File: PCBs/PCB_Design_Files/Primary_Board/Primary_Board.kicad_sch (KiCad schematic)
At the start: 0 parts

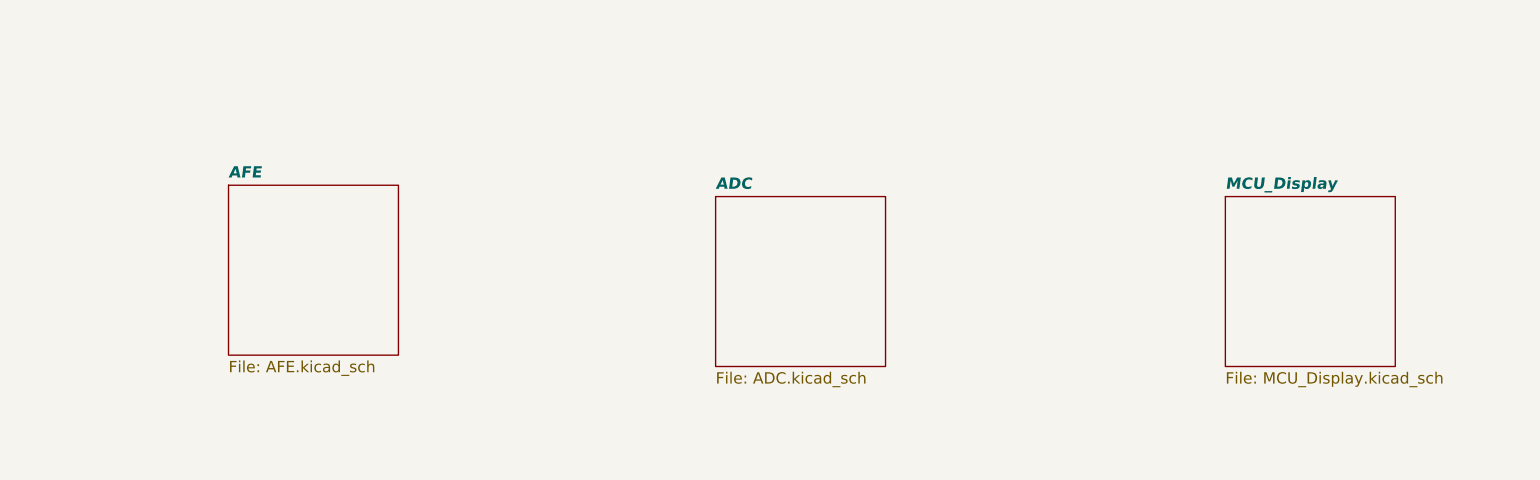
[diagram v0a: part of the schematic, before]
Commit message: AFE schematic, added 0603 component libraries
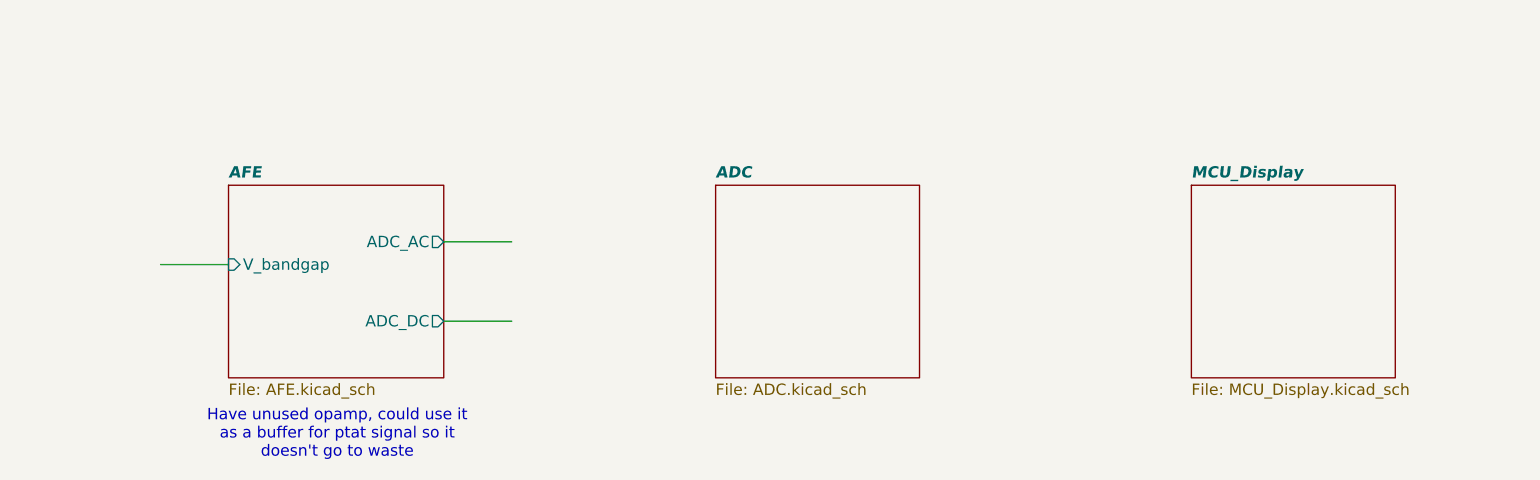
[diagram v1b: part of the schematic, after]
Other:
- sheet AFE ports: added ADC_AC, ADC_DC, V_bandgap; removed none
- note added: "Have unused opamp, could use it as a buffer for ptat signal so it doesn't go to waste"
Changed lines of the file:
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@@
 		(company "ECE115DA/DW Capstone")
+	)
+	(text "Have unused opamp, could use it\nas a buffer for ptat signal so it\ndoesn't go to waste"
+		(exclude_from_sim no)
+		(at 94.742 107.95 0)
+		(effects
+			(font
+				(size 1.27 1.27)
+			)
+		)
 	)
 	(text "Pulse Oximeter Primary Board"
@@
 		)
 	)
+	(wire
+		(pts
+			(xy 106.68 95.25) (xy 114.3 95.25)
+		)
+		(stroke
+			(width 0)
+			(type default)
+		)
+	)
+	(wire
+		(pts
+			(xy 74.93 88.9) (xy 82.55 88.9)
+		)
+		(stroke
+			(width 0)
+			(type default)
+		)
+	)
+	(wire
+		(pts
+			(xy 106.68 86.36) (xy 114.3 86.36)
+		)
+		(stroke
+			(width 0)
+			(type default)
+		)
+	)
 	(sheet
 		(at 82.55 80.01)
-		(size 19.05 19.05)
+		(size 24.13 21.59)
 		(exclude_from_sim no)
 		(in_bom yes)
@@
 		)
 		(property "Sheetfile" "AFE.kicad_sch"
-			(at 82.55 99.6446 0)
+			(at 82.55 102.1846 0)
 			(effects
 				(font
@@
 				)
 				(justify left top)
+			)
+		)
+		(pin "ADC_AC" output
+			(at 106.68 86.36 0)
+			(effects
+				(font
+					(size 1.27 1.27)
+				)
+				(justify right)
+			)
+		)
+		(pin "ADC_DC" output
+			(at 106.68 95.25 0)
+			(effects
+				(font
+					(size 1.27 1.27)
+				)
+				(justify right)
+			)
+		)
+		(pin "V_bandgap" input
+			(at 82.55 88.9 180)
+			(effects
+				(font
+					(size 1.27 1.27)
+				)
+				(justify left)
 			)
 		)
@@
 	)
 	(sheet
-		(at 137.16 81.28)
-		(size 19.05 19.05)
+		(at 137.16 80.01)
+		(size 22.86 21.59)
 		(exclude_from_sim no)
 		(in_bom yes)
@@
 		)
 		(property "Sheetname" "ADC"
-			(at 137.16 80.5684 0)
+			(at 137.16 79.2984 0)
 			(effects
 				(font
@@
 		)
 		(property "Sheetfile" "ADC.kicad_sch"
-			(at 137.16 100.9146 0)
+			(at 137.16 102.1846 0)
 			(effects
 				(font
@@
 	)
 	(sheet
-		(at 194.31 81.28)
-		(size 19.05 19.05)
+		(at 190.5 80.01)
+		(size 22.86 21.59)
 		(exclude_from_sim no)
 		(in_bom yes)
@@
 		)
 		(property "Sheetname" "MCU_Display"
-			(at 194.31 80.5684 0)
+			(at 190.5 79.2984 0)
 			(effects
 				(font
@@
 		)
 		(property "Sheetfile" "MCU_Display.kicad_sch"
-			(at 194.31 100.9146 0)
+			(at 190.5 102.1846 0)
 			(effects
 				(font

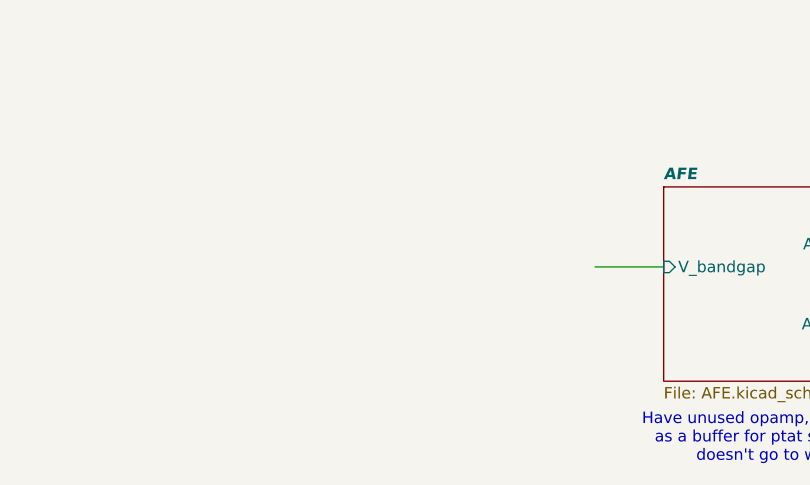
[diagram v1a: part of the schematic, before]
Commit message: added ptat_bandgap subsheet
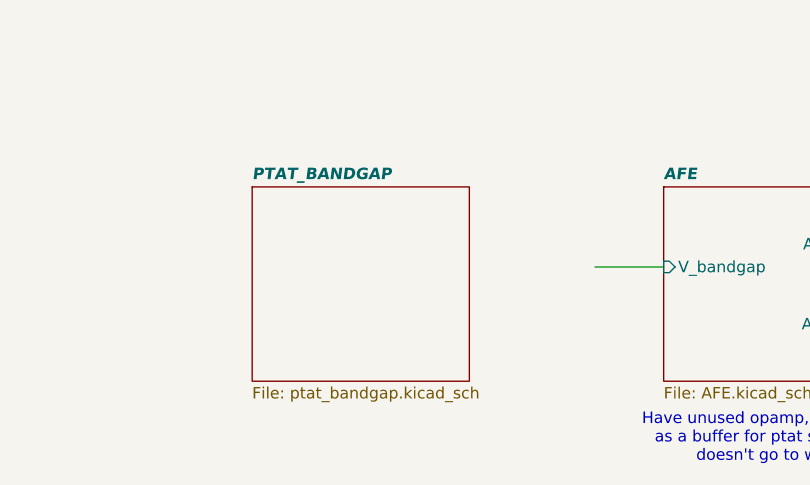
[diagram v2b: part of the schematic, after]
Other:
- added sheet PTAT_BANDGAP (ptat_bandgap.kicad_sch)
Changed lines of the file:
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@@
+		)
+	)
+	(sheet
+		(at 36.83 80.01)
+		(size 24.13 21.59)
+		(exclude_from_sim no)
+		(in_bom yes)
+		(on_board yes)
+		(dnp no)
+		(fields_autoplaced yes)
+		(stroke
+			(width 0.1524)
+			(type solid)
+		)
+		(fill
+			(color 255 229 191 1.0000)
+		)
+		(property "Sheetname" "PTAT_BANDGAP"
+			(at 36.83 79.2984 0)
+			(effects
+				(font
+					(size 1.27 1.27)
+					(thickness 0.254)
+					(bold yes)
+					(italic yes)
+				)
+				(justify left bottom)
+			)
+		)
+		(property "Sheetfile" "ptat_bandgap.kicad_sch"
+			(at 36.83 102.1846 0)
+			(effects
+				(font
+					(size 1.27 1.27)
+				)
+				(justify left top)
+			)
+		)
+		(instances
+			(project "Primary_Board"
+				(path "/8c3d01e8-a984-4e4e-9220-7d351336a99b"
+					(page "5")
+				)
+			)
 		)
 	)

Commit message: ptat_bandgap component libraries
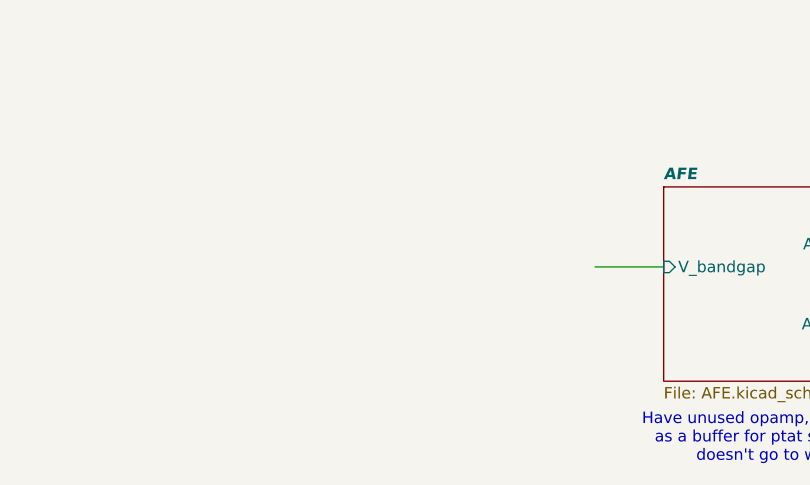
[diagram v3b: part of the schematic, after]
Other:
- removed sheet PTAT_BANDGAP
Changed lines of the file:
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@@
-		)
-	)
-	(sheet
-		(at 36.83 80.01)
-		(size 24.13 21.59)
-		(exclude_from_sim no)
-		(in_bom yes)
-		(on_board yes)
-		(dnp no)
-		(fields_autoplaced yes)
-		(stroke
-			(width 0.1524)
-			(type solid)
-		)
-		(fill
-			(color 255 229 191 1.0000)
-		)
-		(property "Sheetname" "PTAT_BANDGAP"
-			(at 36.83 79.2984 0)
-			(effects
-				(font
-					(size 1.27 1.27)
-					(thickness 0.254)
-					(bold yes)
-					(italic yes)
-				)
-				(justify left bottom)
-			)
-		)
-		(property "Sheetfile" "ptat_bandgap.kicad_sch"
-			(at 36.83 102.1846 0)
-			(effects
-				(font
-					(size 1.27 1.27)
-				)
-				(justify left top)
-			)
-		)
-		(instances
-			(project "Primary_Board"
-				(path "/8c3d01e8-a984-4e4e-9220-7d351336a99b"
-					(page "5")
-				)
-			)
 		)
 	)

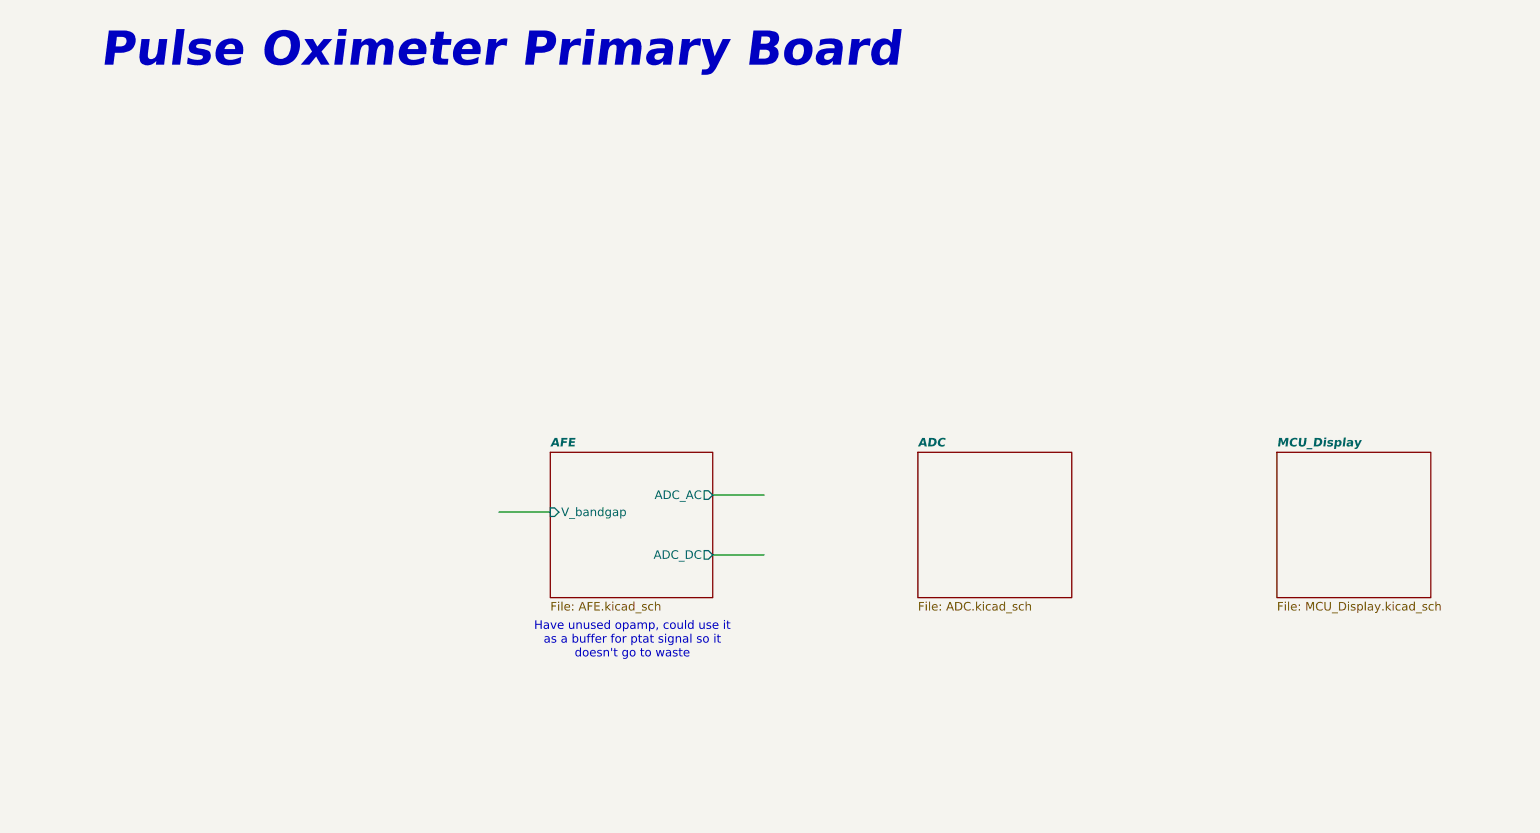
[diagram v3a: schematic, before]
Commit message: Bandgap/Ptat layout on secondary board. Updated grounded mounting holes on schematic, fix all DRC warnings
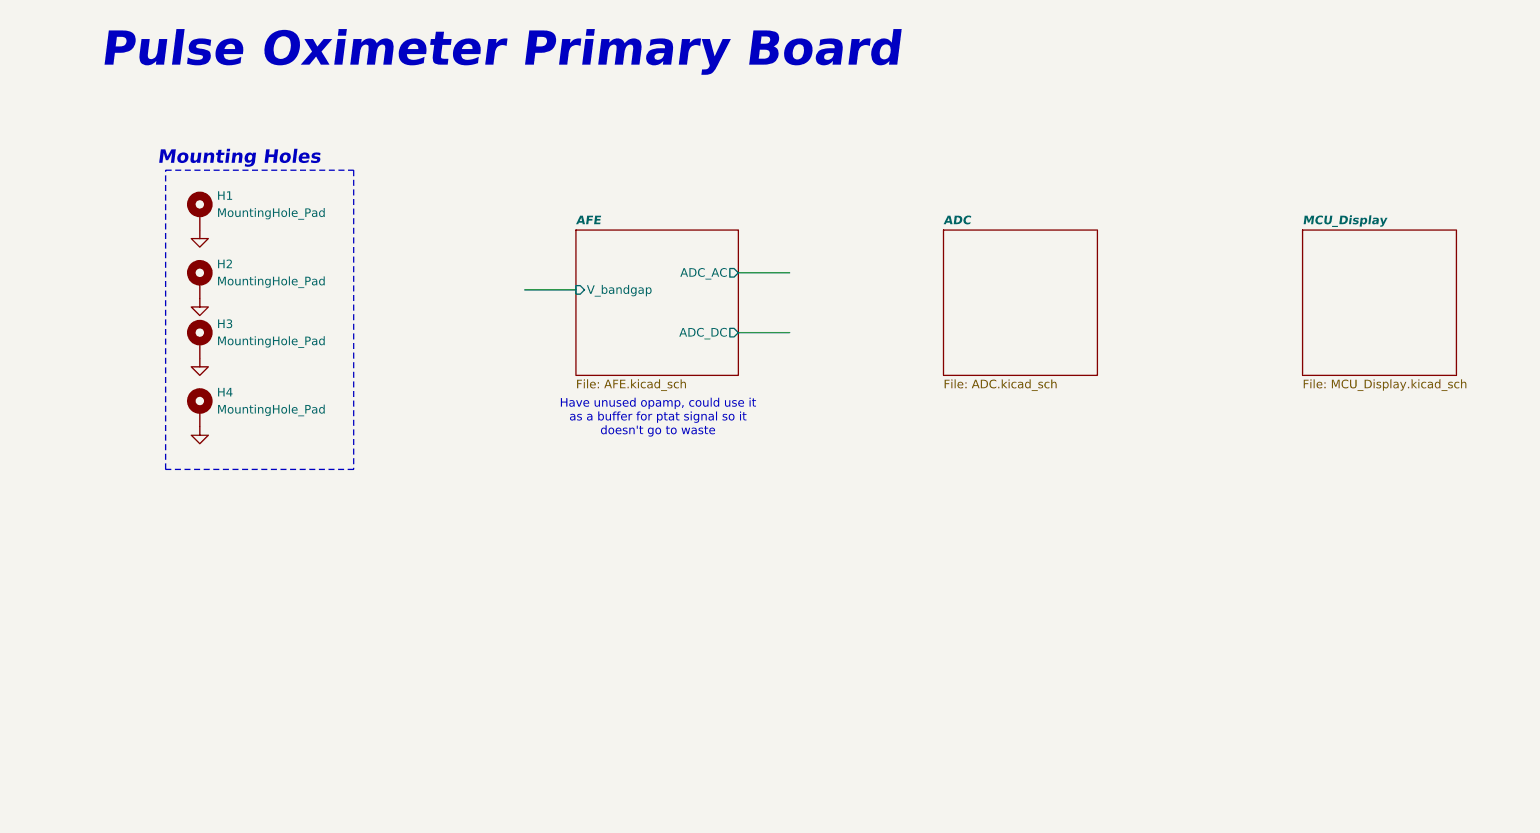
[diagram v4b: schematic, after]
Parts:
- added H1, H2, H3, H4: MountingHole_Pad, MountingHole:MountingHole_2.2mm_M2_DIN965_Pad, symbol Mechanical:MountingHole_Pad
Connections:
- new net GND: H1.1, H2.1, H3.1, H4.1
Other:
- note added: "Mounting Holes"

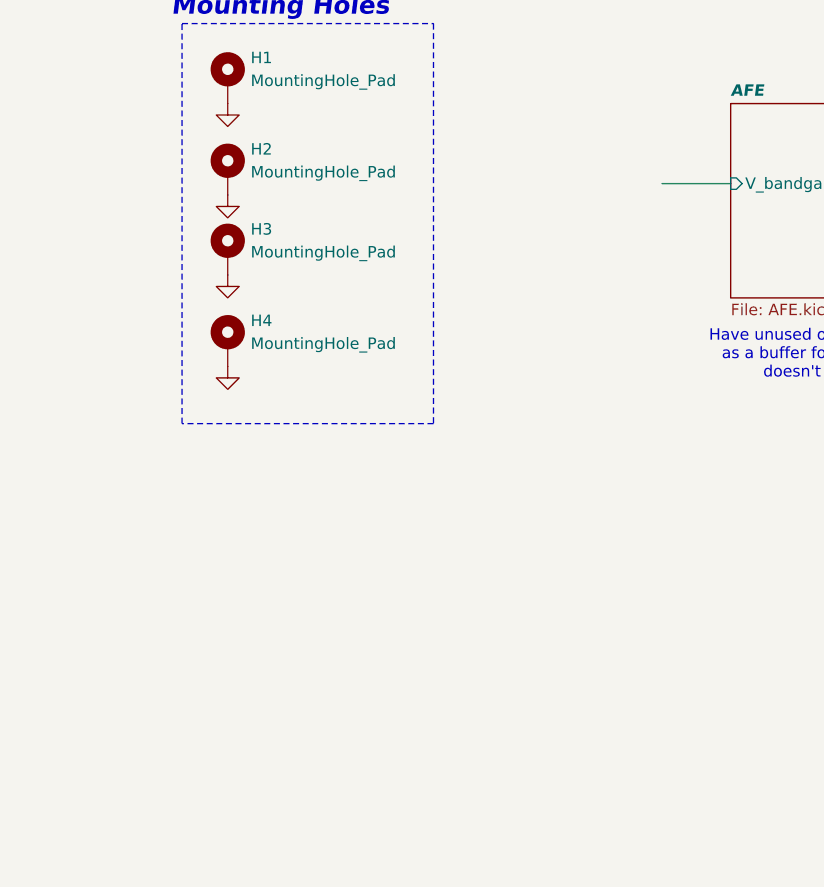
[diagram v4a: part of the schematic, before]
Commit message: Added header and ffc connector to both boards + update libraries. Updated BOM
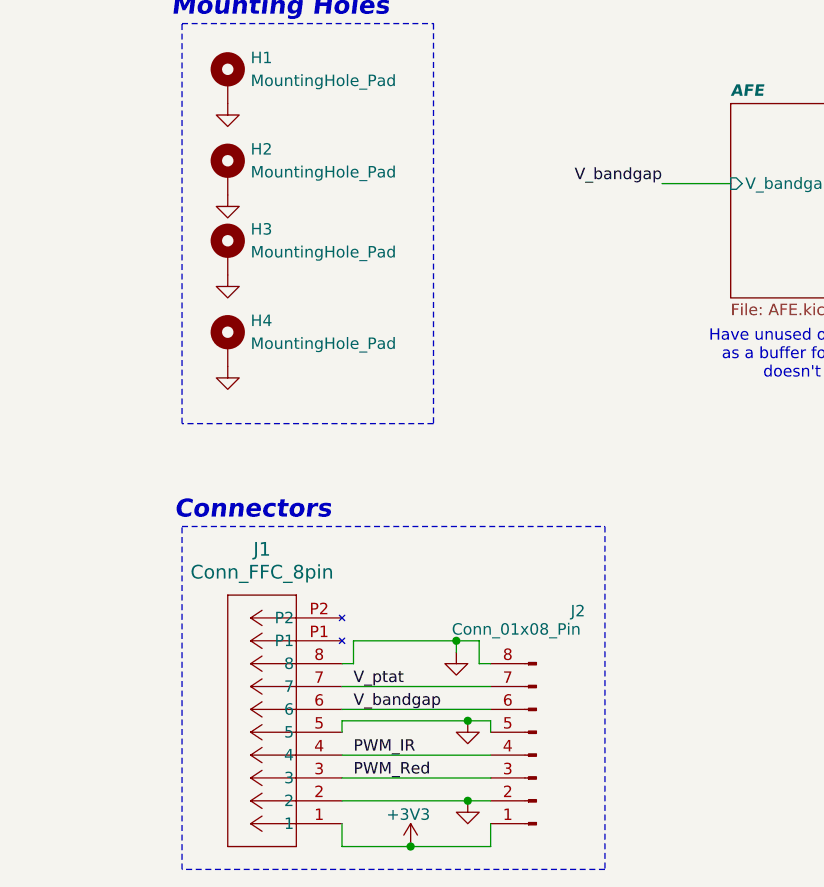
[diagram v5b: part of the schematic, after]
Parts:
- added J1: Conn_FFC_8pin, Project Footprints:Conn_FFC_8pin, symbol Project_Symbols:Conn_FFC_8pin
- added J2: Conn_01x08_Pin, Connector_PinHeader_2.54mm:PinHeader_1x08_P2.54mm_Vertical, symbol Connector:Conn_01x08_Pin
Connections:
- net GND: now also J1.2, J1.5, J1.8, J2.2 (Pin_2), J2.5 (Pin_5), J2.8 (Pin_8)
- new net +3V3: J1.1, J2.1 (Pin_1)
- new net PWM_IR: J1.4, J2.4 (Pin_4)
- new net PWM_Red: J1.3, J2.3 (Pin_3)
- new net V_bandgap: J1.6, J2.6 (Pin_6)
- new net V_ptat: J1.7, J2.7 (Pin_7)
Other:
- note added: "Connectors"

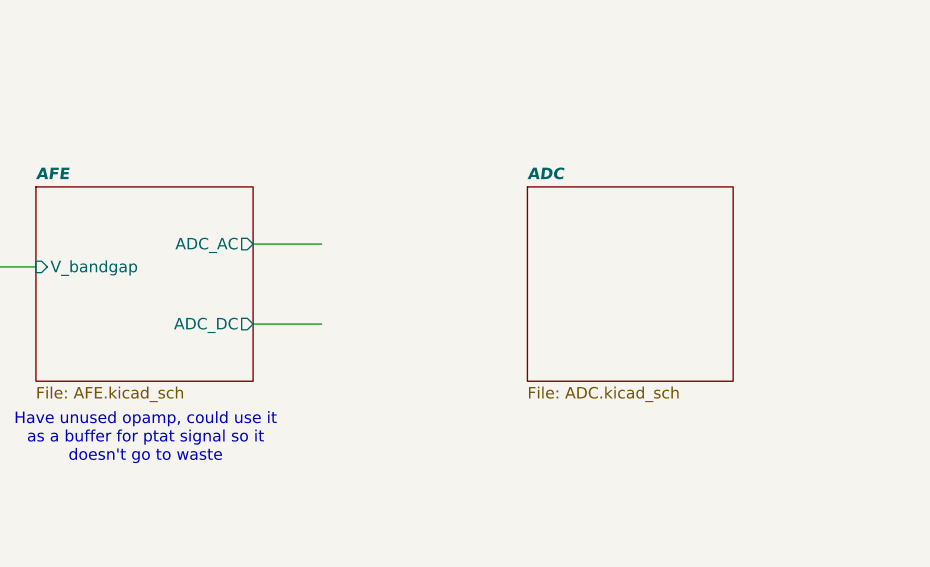
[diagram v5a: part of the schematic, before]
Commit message: added some parts of schematic
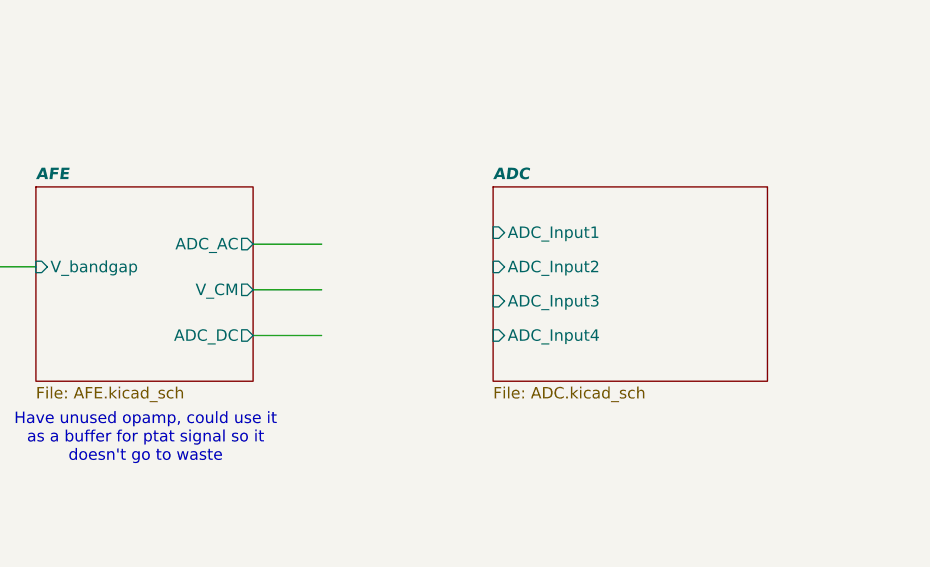
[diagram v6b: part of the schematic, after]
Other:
- sheet ADC ports: added ADC_Input1, ADC_Input2, ADC_Input3, ADC_Input4; removed none
- sheet AFE ports: added V_CM; removed none
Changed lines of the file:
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@@
 	(wire
 		(pts
-			(xy 110.49 62.23) (xy 118.11 62.23)
+			(xy 110.49 63.5) (xy 118.11 63.5)
 		)
 		(stroke
@@
 		(pts
 			(xy 78.74 55.88) (xy 86.36 55.88)
+		)
+		(stroke
+			(width 0)
+			(type default)
+		)
+	)
+	(wire
+		(pts
+			(xy 110.49 58.42) (xy 118.11 58.42)
 		)
 		(stroke
@@
 		)
 		(pin "ADC_DC" output
-			(at 110.49 62.23 0)
+			(at 110.49 63.5 0)
 			(effects
 				(font
@@
 			)
 		)
+		(pin "V_CM" output
+			(at 110.49 58.42 0)
+			(effects
+				(font
+					(size 1.27 1.27)
+				)
+				(justify right)
+			)
+		)
 		(instances
 			(project "Primary_Board"
@@
 	)
 	(sheet
-		(at 140.97 46.99)
-		(size 22.86 21.59)
+		(at 137.16 46.99)
+		(size 30.48 21.59)
 		(exclude_from_sim no)
 		(in_bom yes)
@@
 		)
 		(property "Sheetname" "ADC"
-			(at 140.97 46.2784 0)
+			(at 137.16 46.2784 0)
 			(effects
 				(font
@@
 		)
 		(property "Sheetfile" "ADC.kicad_sch"
-			(at 140.97 69.1646 0)
+			(at 137.16 69.1646 0)
 			(effects
 				(font
@@
 			)
 		)
+		(pin "ADC_Input1" input
+			(at 137.16 52.07 180)
+			(effects
+				(font
+					(size 1.27 1.27)
+				)
+				(justify left)
+			)
+		)
+		(pin "ADC_Input2" input
+			(at 137.16 55.88 180)
+			(effects
+				(font
+					(size 1.27 1.27)
+				)
+				(justify left)
+			)
+		)
+		(pin "ADC_Input3" input
+			(at 137.16 59.69 180)
+			(effects
+				(font
+					(size 1.27 1.27)
+				)
+				(justify left)
+			)
+		)
+		(pin "ADC_Input4" input
+			(at 137.16 63.5 180)
+			(effects
+				(font
+					(size 1.27 1.27)
+				)
+				(justify left)
+			)
+		)
